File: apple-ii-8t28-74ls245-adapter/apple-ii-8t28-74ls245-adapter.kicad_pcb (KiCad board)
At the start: 2 copper layers, 51.6 x 33.8 mm, 4 parts, among them J1 8T28 H11, J2 8T28 H10, U1 74LS245

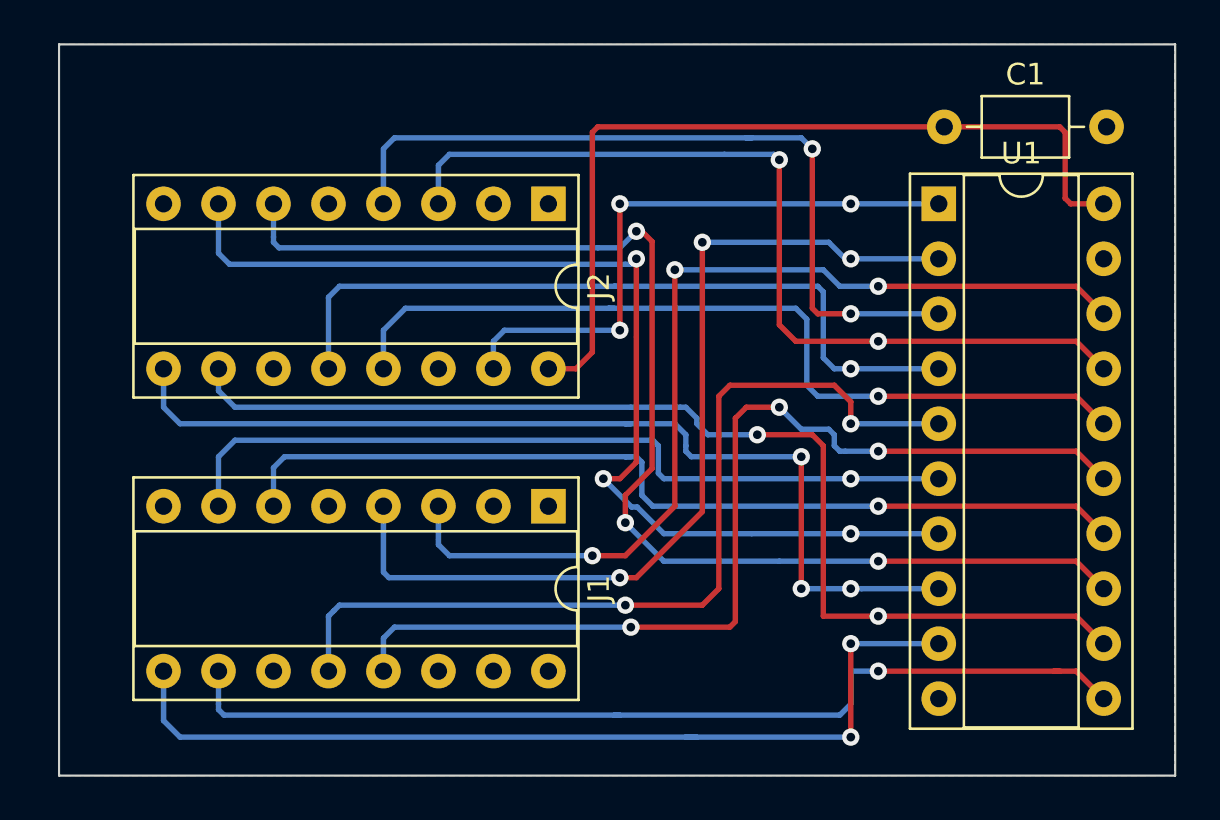
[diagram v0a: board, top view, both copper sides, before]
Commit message: Move some silkscreen bits around to hopefully look better
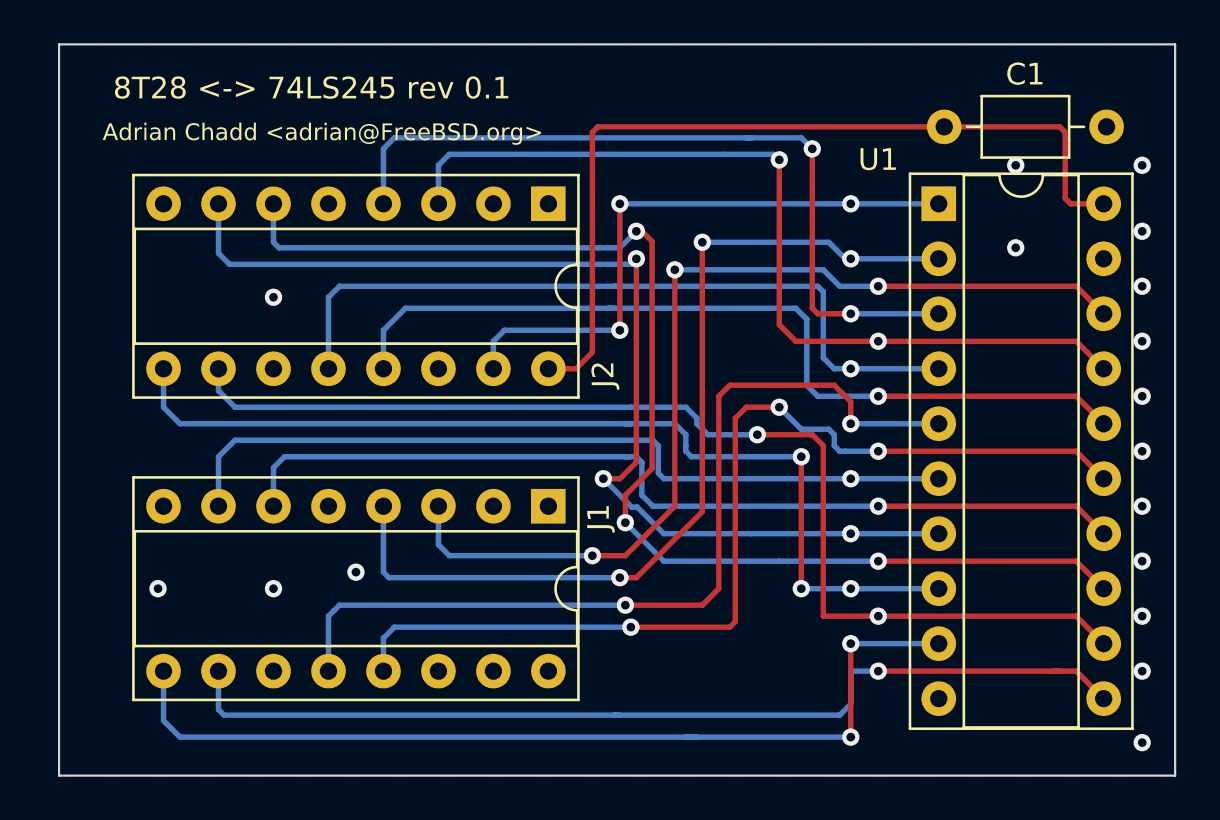
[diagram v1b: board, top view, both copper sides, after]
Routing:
- net GND: vias 0 -> 17
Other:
- board text added: "8T28 <-> 74LS245 rev 0.1"
- board text added: "Adrian Chadd <adrian@FreeBSD.org>"
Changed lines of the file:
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@@
   (general
     (thickness 1.6)
-    (drawings 4)
-    (tracks 275)
+    (drawings 6)
+    (tracks 292)
     (zones 0)
     (modules 4)
@@
   (page A4)
   (layers
-    (0 F.Cu signal)
+    (0 F.Cu signal hide)
     (31 B.Cu signal)
     (32 B.Adhes user)
@@
     (descr "16-lead though-hole mounted DIP package, row spacing 7.62 mm (300 mils), Socket")
     (tags "THT DIP DIL PDIP 2.54mm 7.62mm 300mil Socket")
-    (fp_text reference J1 (at 3.81 -2.33 90) (layer F.SilkS)
+    (fp_text reference J1 (at 0.508 -2.33 90) (layer F.SilkS)
       (effects (font (size 1 1) (thickness 0.15)))
     )
@@
     (descr "16-lead though-hole mounted DIP package, row spacing 7.62 mm (300 mils), Socket")
     (tags "THT DIP DIL PDIP 2.54mm 7.62mm 300mil Socket")
-    (fp_text reference J2 (at 3.81 -2.33 90) (layer F.SilkS)
+    (fp_text reference J2 (at 7.874 -2.54 90) (layer F.SilkS)
       (effects (font (size 1 1) (thickness 0.15)))
     )
@@
     (descr "20-lead though-hole mounted DIP package, row spacing 7.62 mm (300 mils), Socket")
     (tags "THT DIP DIL PDIP 2.54mm 7.62mm 300mil Socket")
-    (fp_text reference U1 (at 3.81 -2.33) (layer F.SilkS)
+    (fp_text reference U1 (at -2.794 -2.032) (layer F.SilkS)
       (effects (font (size 1 1) (thickness 0.15)))
     )
@@
     )
   )
+  (gr_text "Adrian Chadd <adrian@FreeBSD.org>" (at 24.13 16.002) (layer F.SilkS)
+    (effects (font (size 0.7714 0.7714) (thickness 0.15)))
+  )
+  (gr_text "8T28 <-> 74LS245 rev 0.1" (at 23.622 13.97) (layer F.SilkS)
+    (effects (font (size 1 1) (thickness 0.15)))
+  )
   (gr_line (start 63.5 11.938) (end 63.5 45.72) (layer Edge.Cuts) (width 0.1))
   (gr_line (start 11.938 11.938) (end 63.5 11.938) (layer Edge.Cuts) (width 0.1))
@@
   (segment (start 58.674 19.304) (end 60.198 19.304) (width 0.25) (layer F.Cu) (net 1))
   (segment (start 58.42 19.05) (end 58.674 19.304) (width 0.25) (layer F.Cu) (net 1))
+  (via (at 56.134 21.336) (size 0.8) (drill 0.4) (layers F.Cu B.Cu) (net 2))
+  (via (at 56.134 17.526) (size 0.8) (drill 0.4) (layers F.Cu B.Cu) (net 2))
+  (via (at 21.844 23.622) (size 0.8) (drill 0.4) (layers F.Cu B.Cu) (net 2))
+  (via (at 16.51 37.084) (size 0.8) (drill 0.4) (layers F.Cu B.Cu) (net 2))
+  (via (at 21.844 37.084) (size 0.8) (drill 0.4) (layers F.Cu B.Cu) (net 2))
+  (via (at 25.654 36.322) (size 0.8) (drill 0.4) (layers F.Cu B.Cu) (net 2))
+  (via (at 61.976 44.196) (size 0.8) (drill 0.4) (layers F.Cu B.Cu) (net 2))
+  (via (at 61.976 40.894) (size 0.8) (drill 0.4) (layers F.Cu B.Cu) (net 2))
+  (via (at 61.976 38.354) (size 0.8) (drill 0.4) (layers F.Cu B.Cu) (net 2))
+  (via (at 61.976 35.814) (size 0.8) (drill 0.4) (layers F.Cu B.Cu) (net 2))
+  (via (at 61.976 33.274) (size 0.8) (drill 0.4) (layers F.Cu B.Cu) (net 2))
+  (via (at 61.976 30.734) (size 0.8) (drill 0.4) (layers F.Cu B.Cu) (net 2))
+  (via (at 61.976 28.194) (size 0.8) (drill 0.4) (layers F.Cu B.Cu) (net 2))
+  (via (at 61.976 25.654) (size 0.8) (drill 0.4) (layers F.Cu B.Cu) (net 2))
+  (via (at 61.976 23.114) (size 0.8) (drill 0.4) (layers F.Cu B.Cu) (net 2))
+  (via (at 61.976 20.574) (size 0.8) (drill 0.4) (layers F.Cu B.Cu) (net 2))
+  (via (at 61.976 17.526) (size 0.8) (drill 0.4) (layers F.Cu B.Cu) (net 2))
   (via (at 49.784 23.114) (size 0.8) (drill 0.4) (layers F.Cu B.Cu) (net 7))
   (via (at 49.784 25.654) (size 0.8) (drill 0.4) (layers F.Cu B.Cu) (net 25))

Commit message: Update PCB layout - space the vias out a little more!
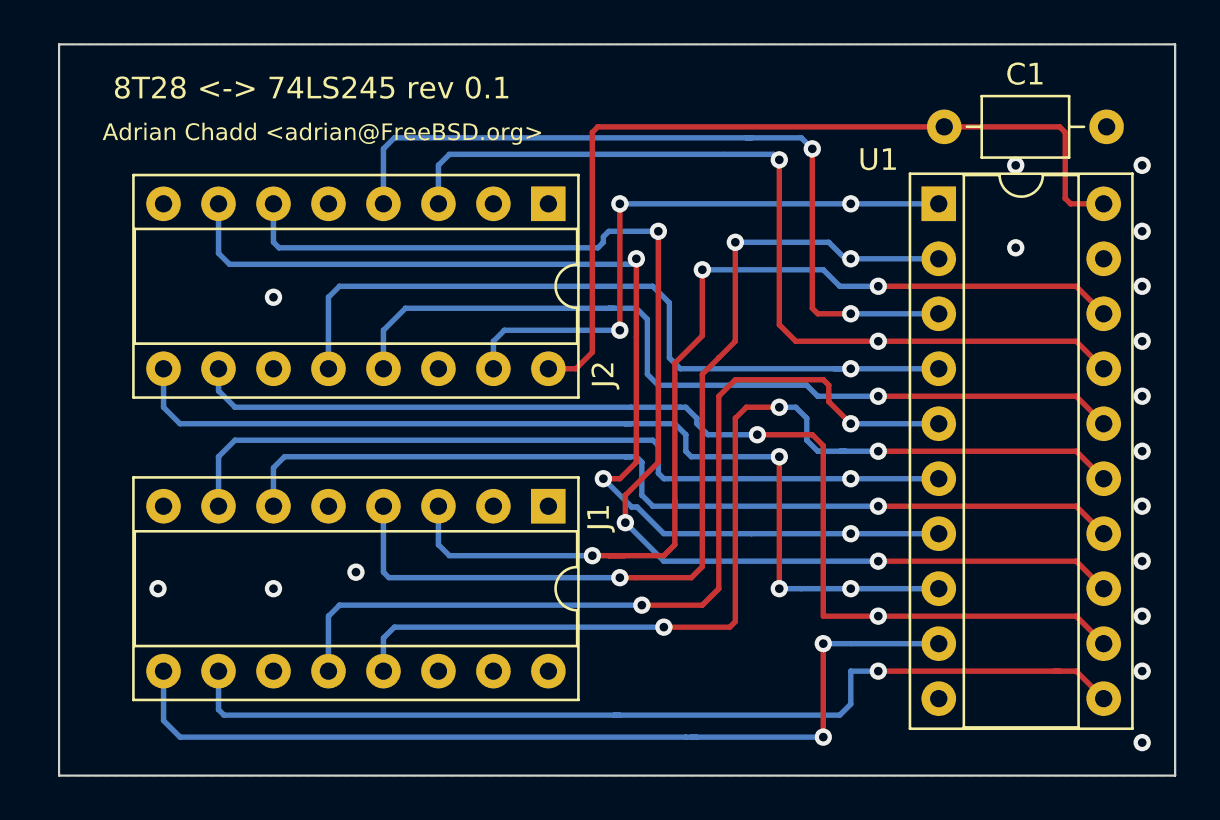
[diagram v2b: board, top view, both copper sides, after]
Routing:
- net CPU_D0: track 45.4 -> 46.7 mm
- net CPU_D5: track 56.7 -> 57.6 mm
- net BUS_D0: track 42.8 -> 43.4 mm
- net CPU_D3: track 46.4 -> 46.9 mm
